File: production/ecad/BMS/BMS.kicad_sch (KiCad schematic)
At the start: 11 parts, among them J11 2147210040, J7 ADC-028-1-T/R-PA10T, U4 TPS75233QPWPREP

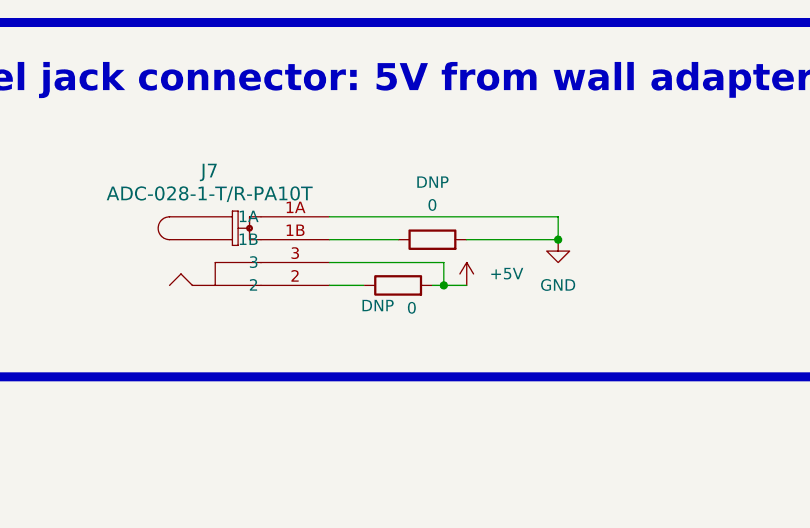
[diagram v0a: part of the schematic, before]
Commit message: All footprints for components + passives from BMS are assigned and ready for layout
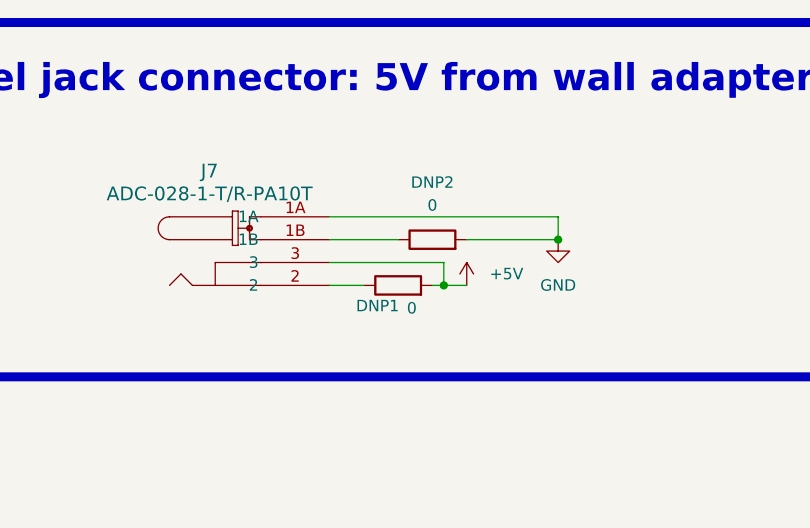
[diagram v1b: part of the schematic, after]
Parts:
- C1, C2: footprint (none) -> Capacitor_SMD:C_0603_1608Metric
- DNP1, DNP2: renamed from DNP; footprint (none) -> Resistor_SMD:R_0201_0603Metric
- R1, R2, R8, R9: footprint (none) -> Resistor_SMD:R_0201_0603Metric
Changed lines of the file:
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@@
 		(dnp no)
 		(fields_autoplaced yes)
-		(property "Reference" "DNP"
+		(property "Reference" "DNP2"
 			(at 237.49 34.29 90)
 			(effects
@@
 			)
 		)
-		(property "Footprint" ""
+		(property "Footprint" "Resistor_SMD:R_0201_0603Metric"
 			(at 237.49 42.418 90)
 			(effects
@@
 			(project "Main"
 				(path "/a34d77bc-8f6a-417e-a206-3165e6c5c658/8907b1b2-1248-4544-8d7d-33764869f691"
-					(reference "DNP")
+					(reference "DNP2")
 					(unit 1)
 				)
@@
 			)
 		)
-		(property "Footprint" ""
+		(property "Footprint" "Resistor_SMD:R_0201_0603Metric"
 			(at 76.962 87.63 90)
 			(effects
@@
 			)
 		)
-		(property "Footprint" ""
+		(property "Footprint" "Resistor_SMD:R_0201_0603Metric"
 			(at 66.802 67.31 90)
 			(effects
@@
 			)
 		)
-		(property "Footprint" ""
+		(property "Footprint" "Resistor_SMD:R_0201_0603Metric"
 			(at 82.042 67.31 90)
 			(effects
@@
 			)
 		)
-		(property "Footprint" ""
+		(property "Footprint" "Capacitor_SMD:C_0603_1608Metric"
 			(at 63.1952 91.44 0)
 			(effects
@@
 		(on_board yes)
 		(dnp no)
-		(property "Reference" "DNP"
+		(property "Reference" "DNP1"
 			(at 231.394 48.006 90)
 			(effects
@@
 			)
 		)
-		(property "Footprint" ""
+		(property "Footprint" "Resistor_SMD:R_0201_0603Metric"
 			(at 233.68 47.498 90)
 			(effects
@@
 			(project "Main"
 				(path "/a34d77bc-8f6a-417e-a206-3165e6c5c658/8907b1b2-1248-4544-8d7d-33764869f691"
-					(reference "DNP")
+					(reference "DNP1")
 					(unit 1)
 				)
@@
 			)
 		)
-		(property "Footprint" ""
+		(property "Footprint" "Capacitor_SMD:C_0603_1608Metric"
 			(at 55.5752 58.42 0)
 			(effects
@@
 			)
 		)
-		(property "Footprint" ""
+		(property "Footprint" "Resistor_SMD:R_0201_0603Metric"
 			(at 82.042 76.2 90)
 			(effects

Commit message: some changes
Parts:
- removed R1: 26.8k, Resistor_SMD:R_0201_0603Metric, symbol Device:R
- C1: footprint Capacitor_SMD:C_0603_1608Metric -> Capacitor_SMD:C_0805_2012Metric
- R1: renamed from R9; value 26.8k -> 53.6k; footprint Resistor_SMD:R_0201_0603Metric -> Resistor_SMD:R_0805_2012Metric
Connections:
- net +3V3: now also R1.2
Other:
- moved on the sheet: R1

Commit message: Component placement complete
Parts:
- J11: footprint 2147210040:MOLEX_2147210040 -> Footprints:4positionheader
- J7: footprint ADC-028-x-T/R-PA10T_ADM -> Footprints:ADC-028-x-T&slash_R-PA10T_ADM
- U4: footprint TPS75233QPWPREP:TPS75233QPWPREP -> Footprints:TPS75233QPWPREP
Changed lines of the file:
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@@
 			)
 		)
-		(property "Footprint" "ADC-028-x-T/R-PA10T_ADM"
+		(property "Footprint" "Footprints:ADC-028-x-T&slash_R-PA10T_ADM"
 			(at 226.06 38.1 0)
 			(effects
@@
 			)
 		)
-		(property "Footprint" "2147210040:MOLEX_2147210040"
+		(property "Footprint" "Footprints:4positionheader"
 			(at 57.15 142.24 0)
 			(effects
@@
 			)
 		)
-		(property "Footprint" "TPS75233QPWPREP:TPS75233QPWPREP"
+		(property "Footprint" "Footprints:TPS75233QPWPREP"
 			(at 118.11 59.69 0)
 			(effects

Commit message: schematic changes and pcb
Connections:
- net GND: now also J11.S1 (SHIELD), J11.S2 (SHIELD)
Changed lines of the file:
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@@
+	)
+	(symbol
+		(lib_id "power:GND")
+		(at 52.07 149.86 0)
+		(unit 1)
+		(exclude_from_sim no)
+		(in_bom yes)
+		(on_board yes)
+		(dnp no)
+		(fields_autoplaced yes)
+		(property "Reference" "#PWR063"
+			(at 52.07 156.21 0)
+			(effects
+				(font
+					(size 1.27 1.27)
+				)
+				(hide yes)
+			)
+		)
+		(property "Value" "GND"
+			(at 52.07 154.94 0)
+			(effects
+				(font
+					(size 1.27 1.27)
+				)
+			)
+		)
+		(property "Footprint" ""
+			(at 52.07 149.86 0)
+			(effects
+				(font
+					(size 1.27 1.27)
+				)
+				(hide yes)
+			)
+		)
+		(property "Datasheet" ""
+			(at 52.07 149.86 0)
+			(effects
+				(font
+					(size 1.27 1.27)
+				)
+				(hide yes)
+			)
+		)
+		(property "Description" "Power symbol creates a global label with name \"GND\" , ground"
+			(at 52.07 149.86 0)
+			(effects
+				(font
+					(size 1.27 1.27)
+				)
+				(hide yes)
+			)
+		)
+		(pin "1"
+		)
+		(instances
+			(project ""
+				(path "/a34d77bc-8f6a-417e-a206-3165e6c5c658/8907b1b2-1248-4544-8d7d-33764869f691"
+					(reference "#PWR063")
+					(unit 1)
+				)
+			)
+		)
 	)
 	(symbol

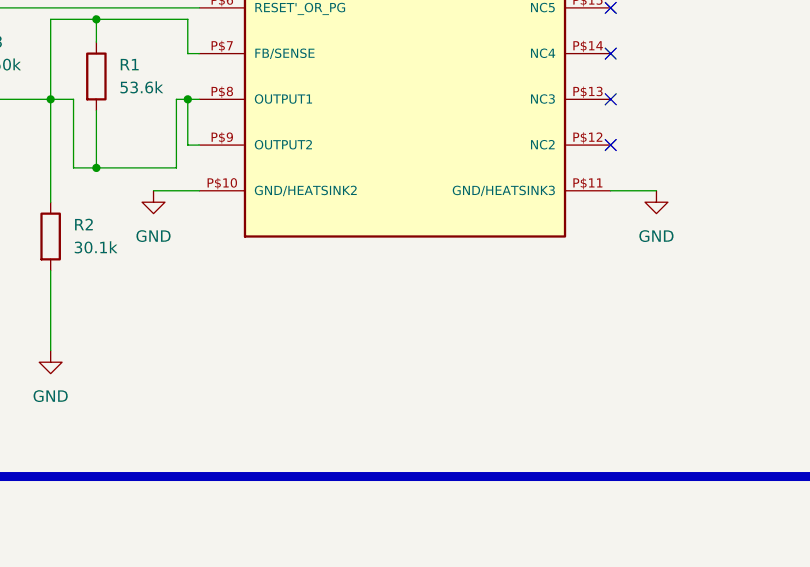
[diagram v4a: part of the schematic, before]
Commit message: Added 3V3, 5V, and GND power planes on layer 2
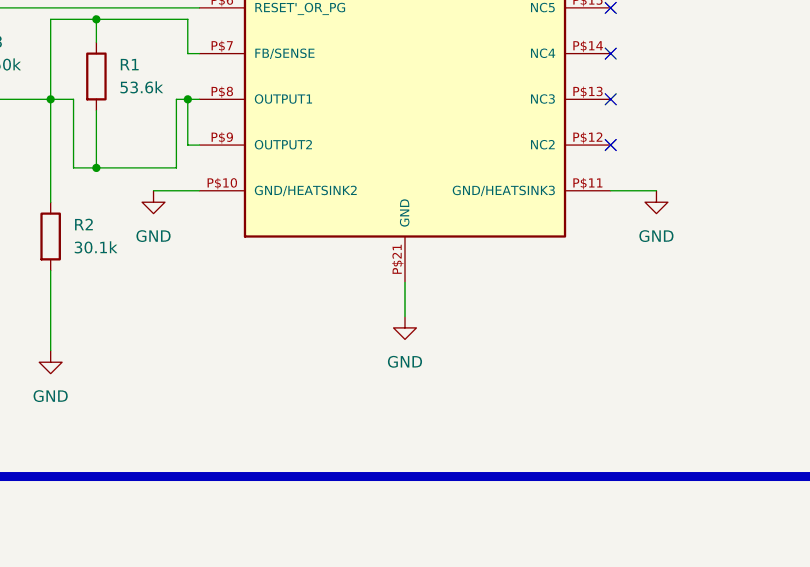
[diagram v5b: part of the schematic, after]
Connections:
- net GND: now also U4.P$21 (GND)
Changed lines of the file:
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@@
+	(wire
+		(pts
+			(xy 118.11 92.71) (xy 118.11 96.52)
+		)
+		(stroke
+			(width 0)
+			(type default)
+		)
+	)
 	(wire
 		(pts
@@
 	(symbol
 		(lib_id "power:GND")
+		(at 118.11 96.52 0)
+		(unit 1)
+		(exclude_from_sim no)
+		(in_bom yes)
+		(on_board yes)
+		(dnp no)
+		(fields_autoplaced yes)
+		(property "Reference" "#PWR067"
+			(at 118.11 102.87 0)
+			(effects
+				(font
+					(size 1.27 1.27)
+				)
+				(hide yes)
+			)
+		)
+		(property "Value" "GND"
+			(at 118.11 101.6 0)
+			(effects
+				(font
+					(size 1.27 1.27)
+				)
+			)
+		)
+		(property "Footprint" ""
+			(at 118.11 96.52 0)
+			(effects
+				(font
+					(size 1.27 1.27)
+				)
+				(hide yes)
+			)
+		)
+		(property "Datasheet" ""
+			(at 118.11 96.52 0)
+			(effects
+				(font
+					(size 1.27 1.27)
+				)
+				(hide yes)
+			)
+		)
+		(property "Description" "Power symbol creates a global label with name \"GND\" , ground"
+			(at 118.11 96.52 0)
+			(effects
+				(font
+					(size 1.27 1.27)
+				)
+				(hide yes)
+			)
+		)
+		(pin "1"
+		)
+		(instances
+			(project ""
+				(path "/a34d77bc-8f6a-417e-a206-3165e6c5c658/8907b1b2-1248-4544-8d7d-33764869f691"
+					(reference "#PWR067")
+					(unit 1)
+				)
+			)
+		)
+	)
+	(symbol
+		(lib_id "power:GND")
 		(at 90.17 82.55 0)
 		(unit 1)
@@
 		(pin "P$5"
 		)
+		(pin "P$21"
+		)
 		(instances

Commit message: footprints
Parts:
- R1: footprint Resistor_SMD:R_0805_2012Metric -> Resistor_SMD:R_0603_1608Metric
- R2, R8: footprint Resistor_SMD:R_0201_0603Metric -> Resistor_SMD:R_0603_1608Metric
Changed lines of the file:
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@@
 			)
 		)
-		(property "Footprint" "Resistor_SMD:R_0201_0603Metric"
+		(property "Footprint" "Resistor_SMD:R_0603_1608Metric"
 			(at 76.962 87.63 90)
 			(effects
@@
 			)
 		)
-		(property "Footprint" "Resistor_SMD:R_0201_0603Metric"
+		(property "Footprint" "Resistor_SMD:R_0603_1608Metric"
 			(at 66.802 67.31 90)
 			(effects
@@
 			)
 		)
-		(property "Footprint" "Resistor_SMD:R_0805_2012Metric"
+		(property "Footprint" "Resistor_SMD:R_0603_1608Metric"
 			(at 82.042 69.85 90)
 			(effects

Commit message: error
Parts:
- DNP1, DNP2: footprint Resistor_SMD:R_0201_0603Metric -> Resistor_SMD:R_0603_1608Metric
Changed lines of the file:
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@@
 			)
 		)
-		(property "Footprint" "Resistor_SMD:R_0201_0603Metric"
+		(property "Footprint" "Resistor_SMD:R_0603_1608Metric"
 			(at 237.49 42.418 90)
 			(effects
@@
 			)
 		)
-		(property "Footprint" "Resistor_SMD:R_0201_0603Metric"
+		(property "Footprint" "Resistor_SMD:R_0603_1608Metric"
 			(at 233.68 47.498 90)
 			(effects

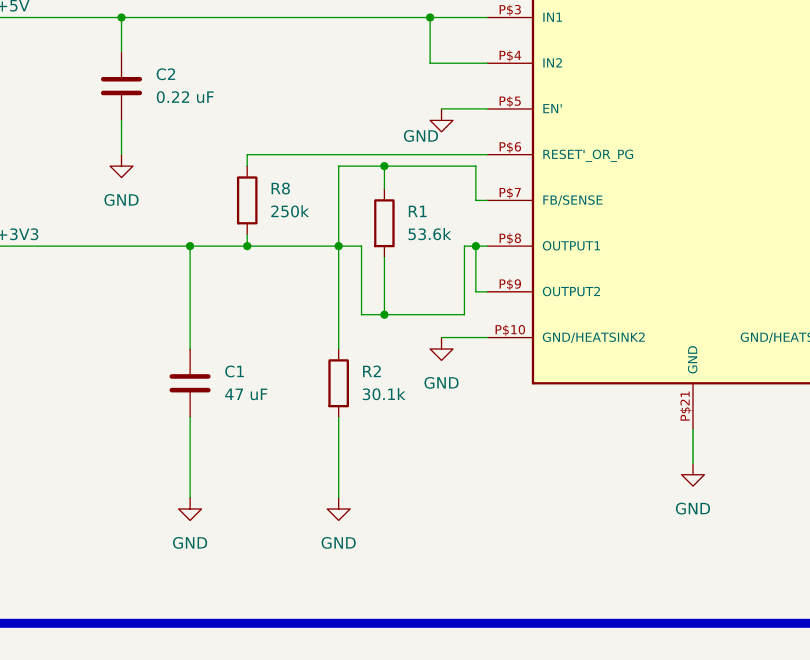
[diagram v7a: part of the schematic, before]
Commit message: moved connectors
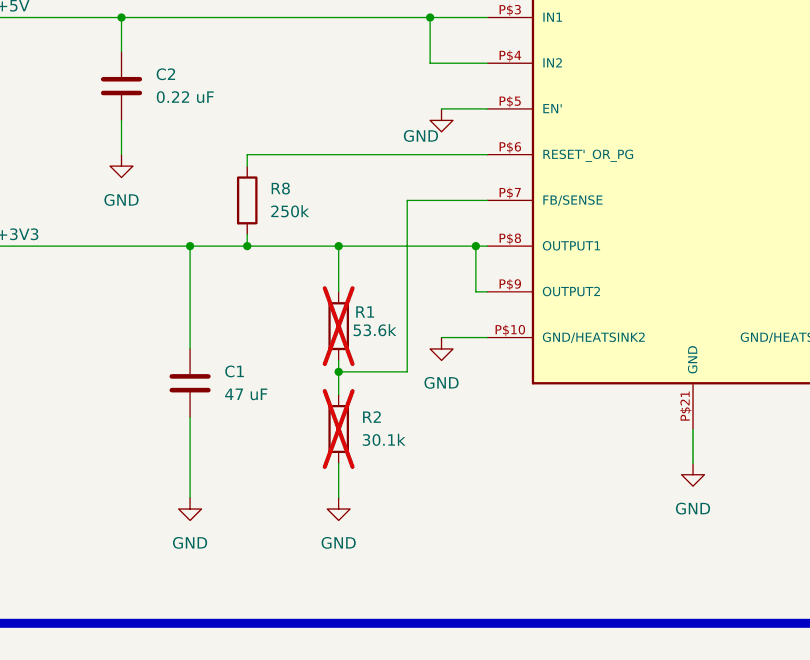
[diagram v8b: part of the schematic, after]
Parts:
- R1, R2: now not fitted
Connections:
- net +3V3: no longer R1.2, R2.1, U4.P$7 (FB/SENSE)
- new net: R1.2, R2.1, U4.P$7 (FB/SENSE)
